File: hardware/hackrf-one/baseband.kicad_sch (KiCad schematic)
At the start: 101 parts, among them P14 XCVR_CLKOUT, P39 SSP1_SCK, P40 SSP1_COPI, P41 SSP1_CIPO, P53 CS_XCVR, P54 CS_AD, P55 TXENABLE, P56 RXENABLE, P61 DA0, P62 DA7, P63 DD0, P64 DD9, P65 DA4, P66 DD5, P67 RSSI, P83 GND, P84 GND, P85 GND, P86 GND, P87 GND, P88 GND, P89 GND, P9 BASEBAND, P90 GND, P91 GND, P92 GND, Q3 MOSFET_P, T3 RX_BALUN, T4 TX_BALUN, U17 MAX2837, U18 MAX5864

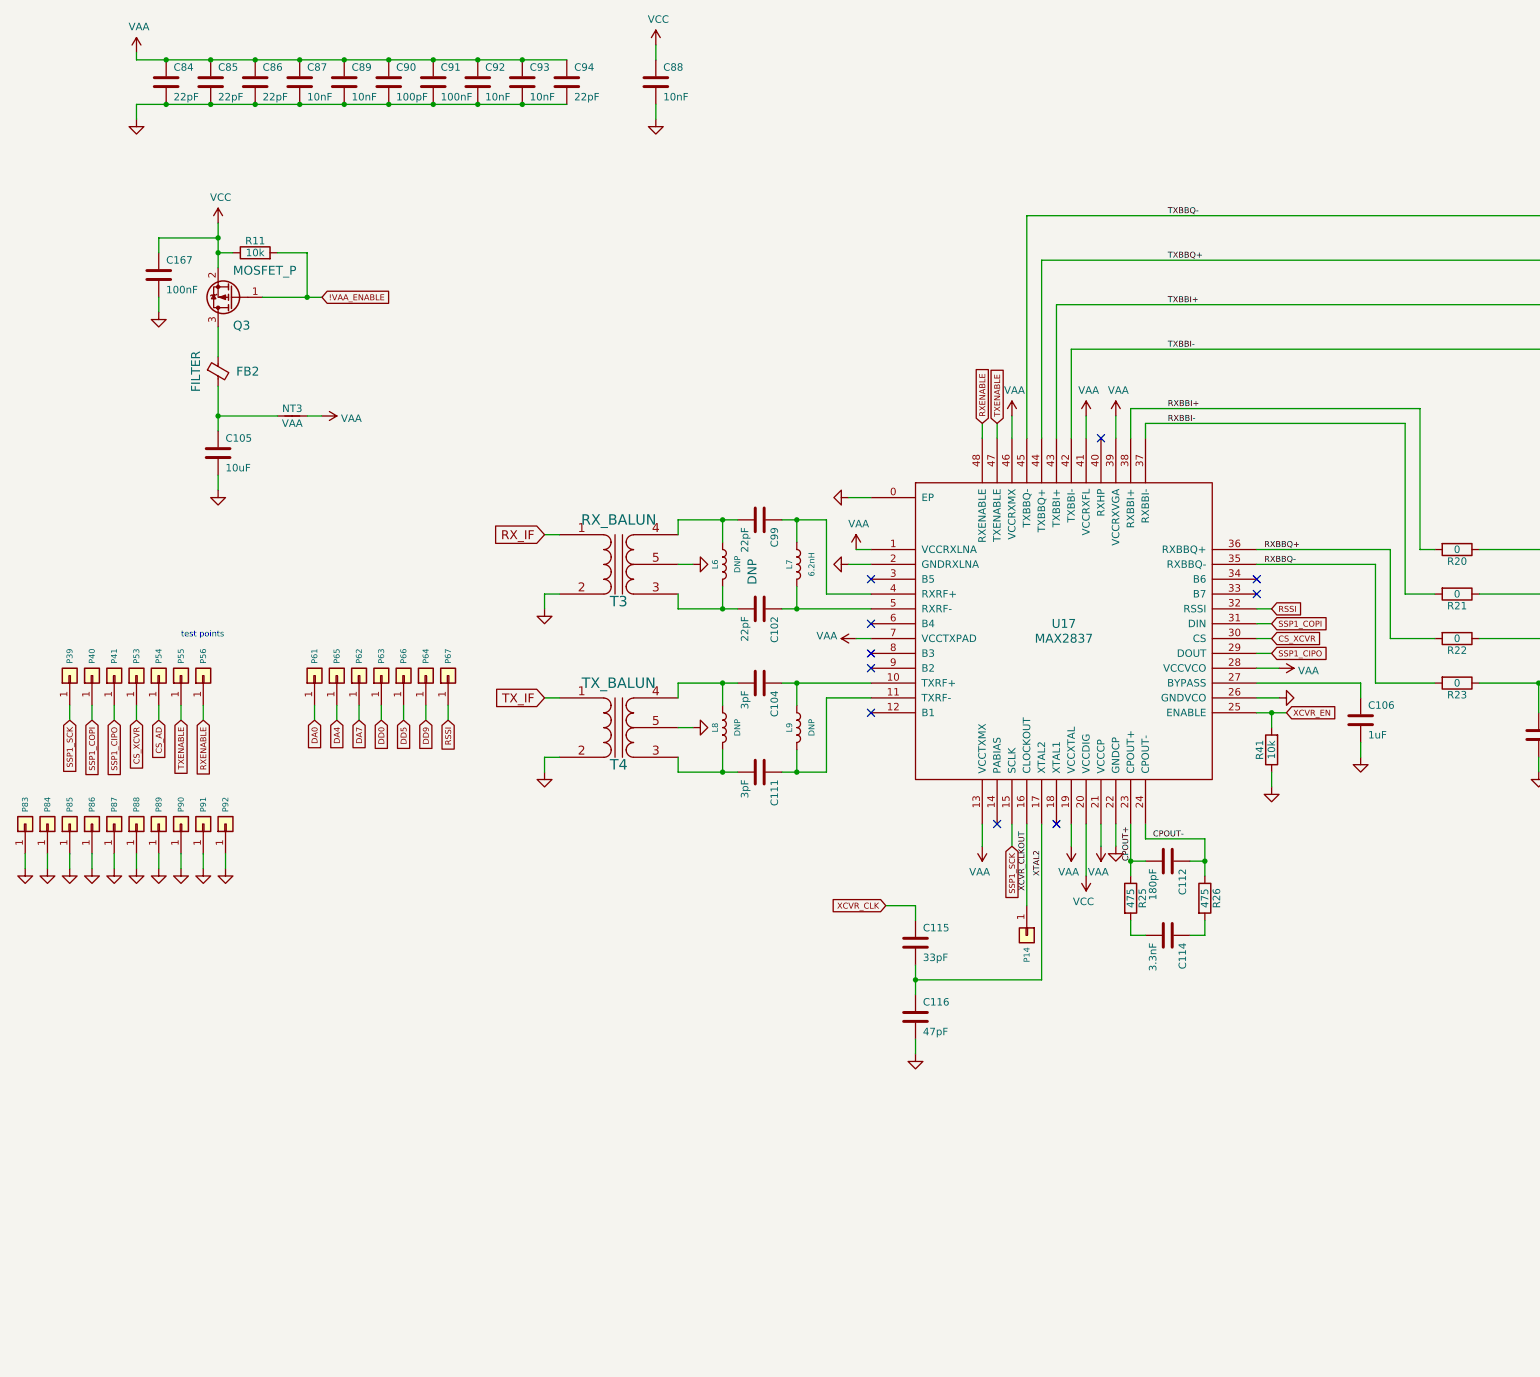
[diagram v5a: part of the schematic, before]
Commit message: HackRF One: change U17 from MAX2837 to MAX2839
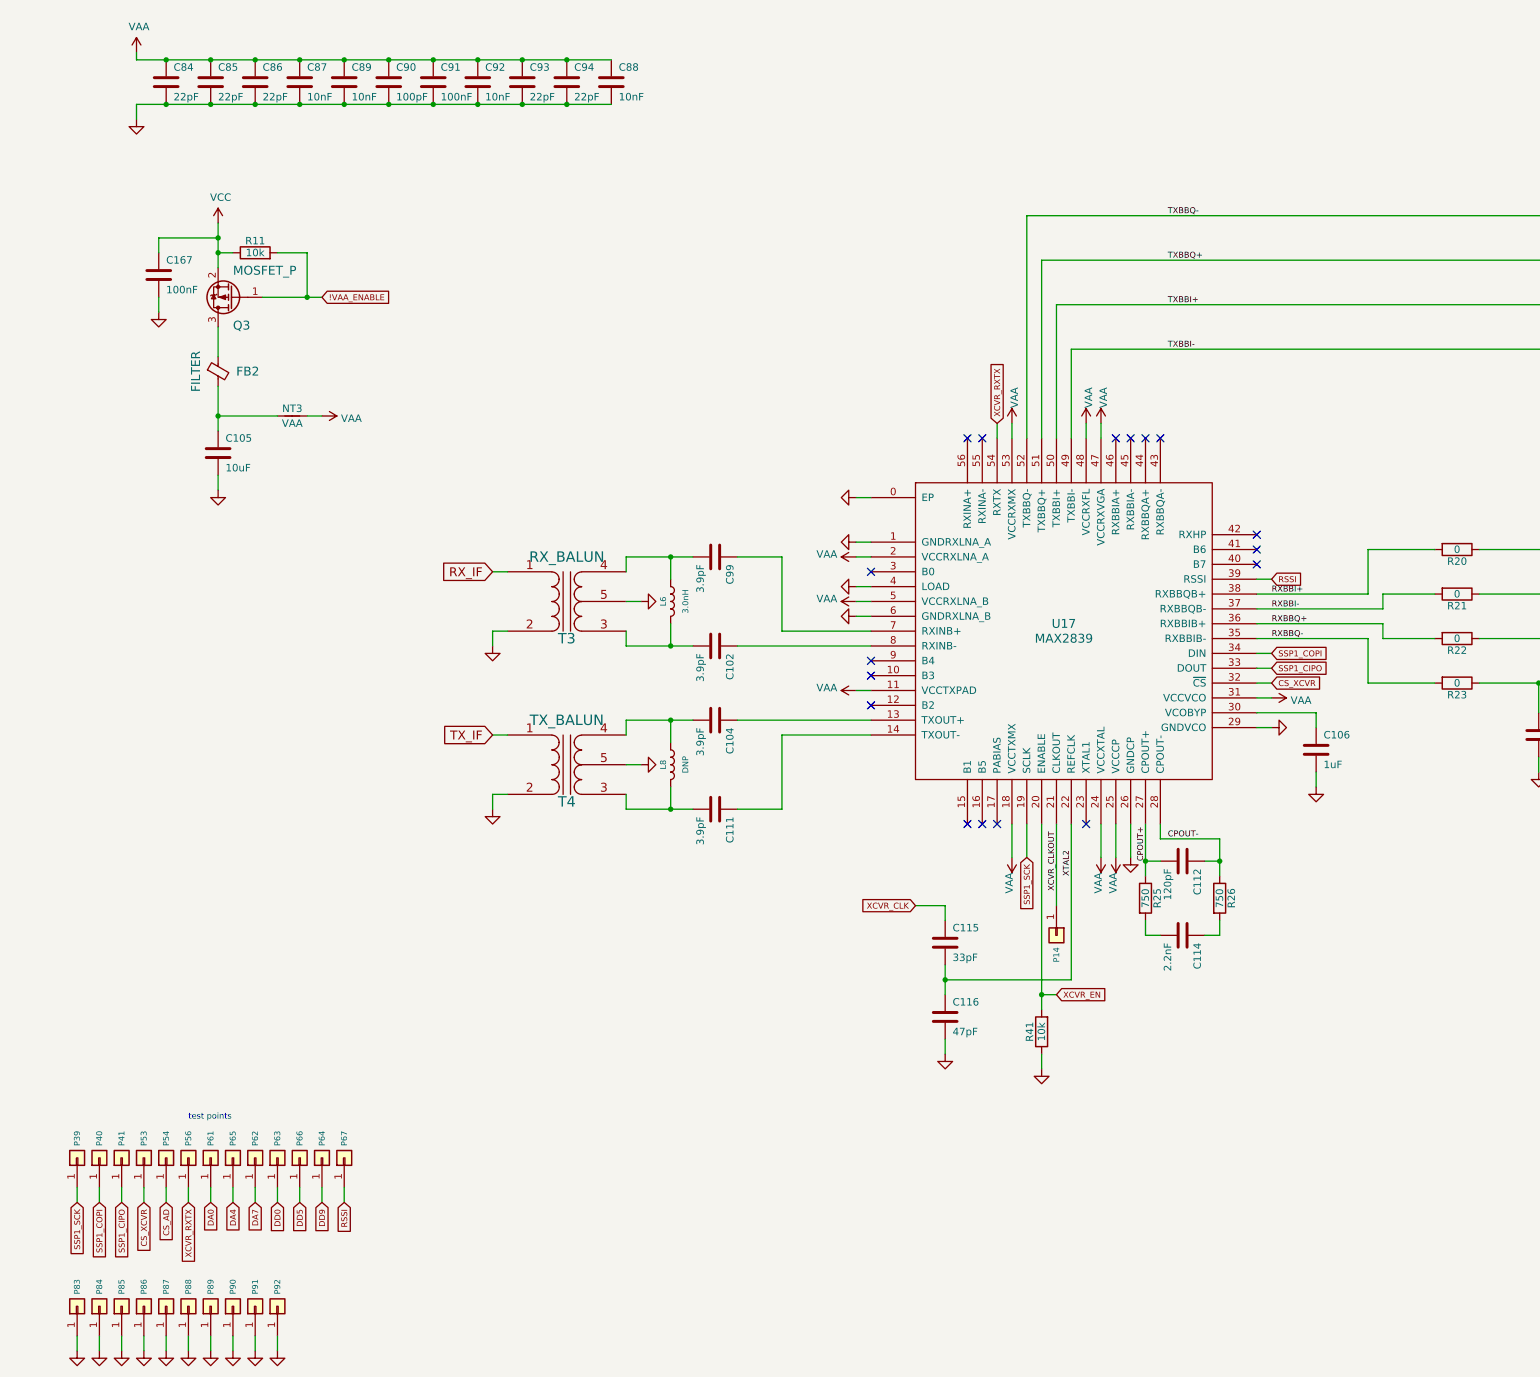
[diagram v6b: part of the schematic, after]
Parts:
- removed L7: 6.2nH, hackrf:GSG-0402, symbol Device:L
- removed L9: DNP, hackrf:GSG-0402, symbol Device:L
- removed P55: TXENABLE, hackrf:GSG-TESTPOINT-50MIL, symbol Connector_Generic:Conn_01x01
- C102, C99: value 22pF -> 3.9pF; Part Number GRM1555C1H220JA01D -> GCM1555C1H3R9BA16D
- C104, C111: value 3pF -> 3.9pF; Part Number GRM1555C1H3R0CA01D -> GCM1555C1H3R9BA16D
- C112: value 180pF -> 120pF; Part Number GRM1555C1H181JA01D -> GCM1555C1H121JA16D
- C114: value 3.3nF -> 2.2nF; Part Number GRM155R71H332KA01D -> GRM155R71H222KA01D
- C93: value 10nF -> 22pF; Part Number GRM155R71C103KA01D -> GRM1555C1H220JA01D
- L6: value DNP -> 3.0nH; Manufacturer (none) -> Murata; Note DNP -> (none); Part Number (none) -> LQG15HS3N0B02D
- R25, R26: value 475 -> 750; Manufacturer Stackpole -> Yageo; Part Number RMCF0402JT470R -> RC0402FR-07750RL
- U17: value MAX2837 -> MAX2839; footprint hackrf:GSG-QFN48-6 -> gsg-modules:QFN-56-1EP_8x8mm_P0.5mm_EP6.5x6.5mm_ThermalVias; symbol hackrf:MAX2837 -> hackrf:MAX2839; Part Number MAX2837ETM+ -> MAX2839ETN+
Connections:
- net TXENABLE is gone; now on net VAA: U17.47 (VCCRXVGA)
- net CPOUT+: now also U17.27 (CPOUT+); no longer U17.23 (CPOUT+)
- net CPOUT-: now also U17.28 (CPOUT-); no longer U17.24 (CPOUT-)
- net CS_XCVR: now also U17.32 (~{CS}); no longer U17.30 (CS)
- net GND: now also U17.1 (GNDRXLNA_A), U17.29 (GNDVCO), U17.4 (LOAD), U17.6 (GNDRXLNA_B); no longer U17.2 (GNDRXLNA), U17.22 (GNDCP)
- net RSSI: now also U17.39 (RSSI); no longer U17.32 (RSSI)
- net SSP1_CIPO: now also U17.33 (DOUT); no longer U17.29 (DOUT)
- net SSP1_COPI: now also U17.34 (DIN); no longer U17.31 (DIN)
- net SSP1_SCK: now also U17.19 (SCLK); no longer U17.15 (SCLK)
- net TXBBI+: now also U17.50 (TXBBI+); no longer U17.43 (TXBBI+)
- net TXBBI-: now also U17.49 (TXBBI-); no longer U17.42 (TXBBI-)
- net TXBBQ+: now also U17.51 (TXBBQ+); no longer U17.44 (TXBBQ+)
- net TXBBQ-: now also U17.52 (TXBBQ-); no longer U17.45 (TXBBQ-)
- net VAA: now also C88.1, U17.11 (VCCTXPAD), U17.18 (VCCTXMX), U17.2 (VCCRXLNA_A), U17.24 (VCCXTAL), U17.25 (VCCCP), U17.31 (VCCVCO), U17.48 (VCCRXFL), U17.5 (VCCRXLNA_B), U17.53 (VCCRXMX); no longer U17.1 (VCCRXLNA), U17.13 (VCCTXMX), U17.19 (VCCXTAL), U17.21 (VCCCP), U17.28 (VCCVCO), U17.39 (VCCRXVGA), U17.41 (VCCRXFL), U17.46 (VCCRXMX), U17.7 (VCCTXPAD)
- net VCC: no longer C88.1, U17.20 (VCCDIG)
- net XCVR_CLKOUT: now also U17.21 (CLKOUT); no longer U17.16 (CLOCKOUT)
- net XCVR_EN: now also U17.20 (ENABLE); no longer U17.25 (ENABLE)
- net XTAL2: now also U17.22 (REFCLK); no longer U17.17 (XTAL2)
- net at U17.10 (B3): no longer C104.1
- net at C111.1: now also U17.14 (TXOUT-); no longer U17.11 (TXRF-)
- net at C106.1: now also U17.30 (VCOBYP); no longer U17.27 (BYPASS)
- net at C99.1: now also U17.7 (RXINB+); no longer U17.4 (RXRF+)
- net at C102.1: now also U17.8 (RXINB-); no longer U17.5 (RXRF-)
- net RXENABLE renamed XCVR_RXTX
- net XCVR_RXTX: now also U17.54 (RXTX); no longer U17.48 (RXENABLE)
- new net: C104.1, U17.13 (TXOUT+)
- no-connect marks 10 -> 17
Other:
- moved on the sheet: C102, C104, C106, C111, C112, C114, C115, C116, C88, C99, L6, L8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

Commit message: HackRF One: component selections, DNP, and Notes
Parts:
- C100, C97, C98: Manufacturer Murata -> Yageo; Part Number GRM155R61A334KE15D -> CC0402KRX5R6BB334
- C101, C103, C107, C108, C109, C110, C95, C96: DNP (none) -> DNP; Manufacturer Murata -> Samsung; Note DNP -> (none); Part Number GRM1555C1H220JA01D -> CL05C220JB5NNNC
- C105: Manufacturer Murata -> Samsung; Part Number GRM21BR61A106KE19L -> CL21A106KOQNNNE
- C106: Manufacturer Taiyo Yuden -> Samsung; Part Number LMK105BJ105KV-F -> CL05A105KP5NNNC
- C115: Manufacturer Murata -> Samsung; Part Number GRM1555C1H330JA01D -> CL05C330JB5NNNC
- C116: Manufacturer Murata -> Samsung; Part Number GRM1555C1H470JA01D -> CL05C470JB5NNNC
- C84, C85, C86, C93, C94: Manufacturer Murata -> Samsung; Part Number GRM1555C1H220JA01D -> CL05C220JB5NNNC
- C87, C88, C89, C92: Manufacturer Murata -> Samsung; Part Number GRM155R71C103KA01D -> CL05B103KB5NNNC
- C90: Manufacturer Murata -> Samsung; Part Number GRM1555C1H101JA01D -> CL05C101JB5NNNC
- L8, NT3, P14, P39, P40, P41, P53, P54, P56, P61, P62, P63, P64, P65, P66, P67, P83, P84, P85, P86, P87, P88, P89, P90, P91, P92: DNP (none) -> DNP; Note DNP -> (none)
- Q3: Manufacturer Diodes Inc. -> Yangzhou Yangjie; Part Number DMP2305U-7 -> YJL2301C
- T3: Note (none) -> Alternative part: Murata LDB182G4510G-120; Note: Alternative part: Murata LDB182G4510G-120 -> (none)
